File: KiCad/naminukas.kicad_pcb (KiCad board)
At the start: 2 copper layers, 10 parts, among them U1 TPSM63606RDLR

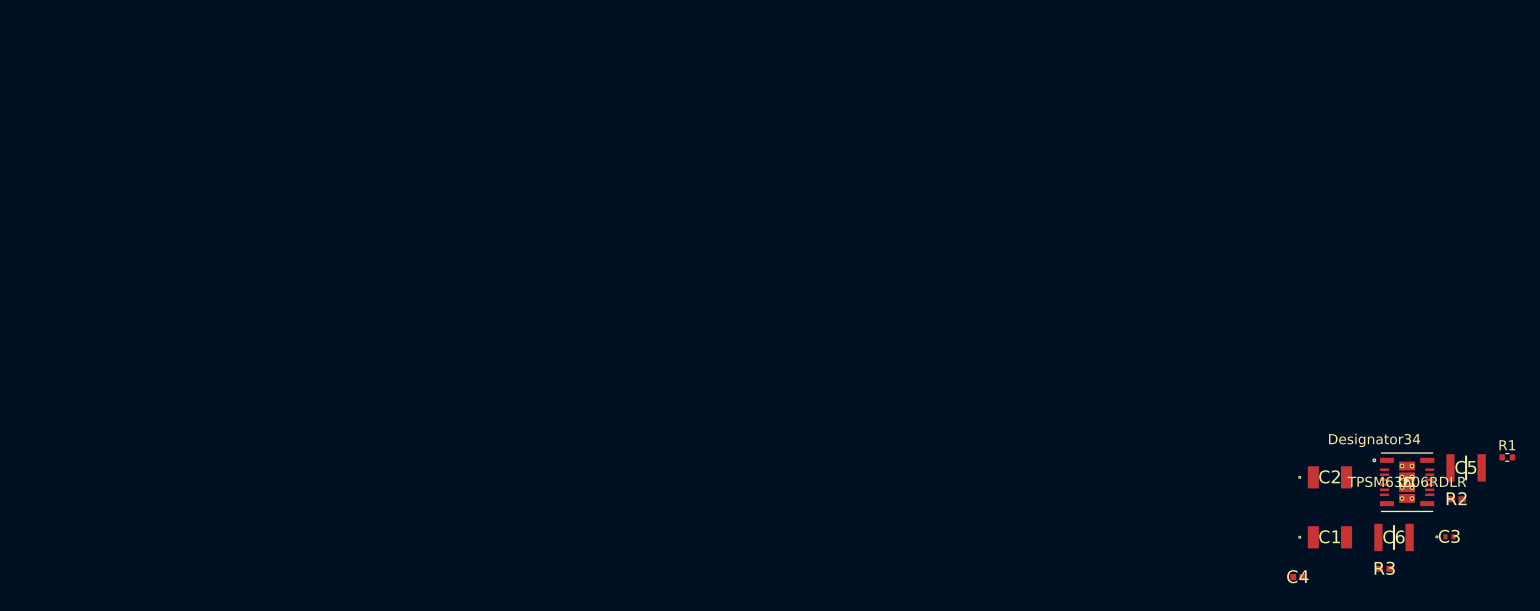
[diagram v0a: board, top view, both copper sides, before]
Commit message: feat(pcb): add mounting holes
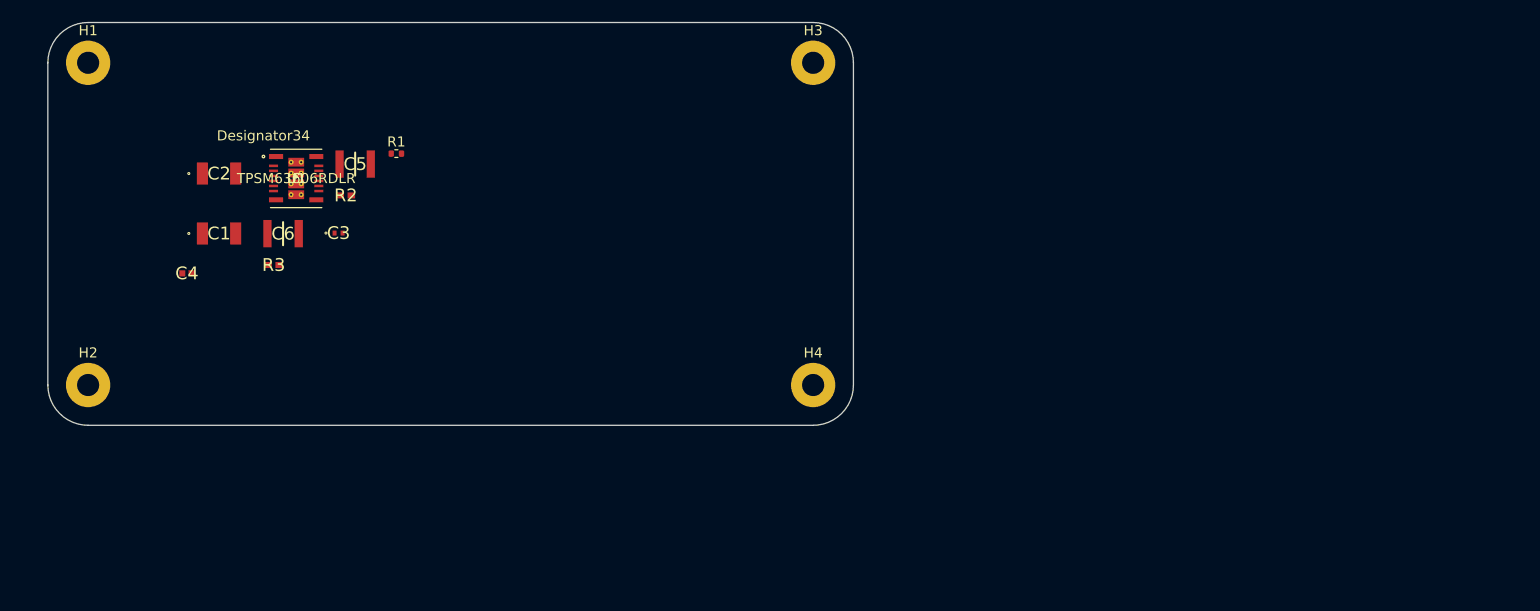
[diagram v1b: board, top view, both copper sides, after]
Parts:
- added H1: Mounting hole, MountingHole:MountingHole_2.2mm_M2_Pad, F.Cu at (24.0, 24.0)
- added H2: Mounting hole, MountingHole:MountingHole_2.2mm_M2_Pad, F.Cu at (24.0, 56.0)
- added H3: Mounting hole, MountingHole:MountingHole_2.2mm_M2_Pad, F.Cu at (96.0, 24.0)
- added H4: Mounting hole, MountingHole:MountingHole_2.2mm_M2_Pad, F.Cu at (96.0, 56.0)
- moved U1 114.4 mm to (44.7, 35.5)
- moved C6 114.4 mm to (43.4, 41.0)
- moved R1 114.4 mm to (54.6, 33.0)
- moved R3 114.4 mm to (42.4, 44.1)
- moved C1 114.4 mm to (37.0, 41.0)
- moved C2 114.4 mm to (37.0, 35.0)
- moved C3 114.4 mm to (48.9, 40.9)
- moved C4 114.4 mm to (33.8, 44.9)
- moved C5 114.4 mm to (50.5, 34.1)
- moved R2 114.4 mm to (49.6, 37.2)
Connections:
- C1 pad 1: GNDREF -> GND
- C2 pad 1: GNDREF -> GND
- C3 pad 1: GNDREF -> GND
- C5 pad 1: GNDREF -> GND
- C6 pad 1: GNDREF -> GND
- R1 pad 2: GNDREF -> GND
- R3 pad 1: GNDREF -> GND
- U1 pad 17: GNDREF -> GND
- U1 pad 18: GNDREF -> GND
- U1 pad 19: GNDREF -> GND
- U1 pad 20: GNDREF -> GND
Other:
- board outline added: 80 x 40 mm
- copper layers 2 -> 4

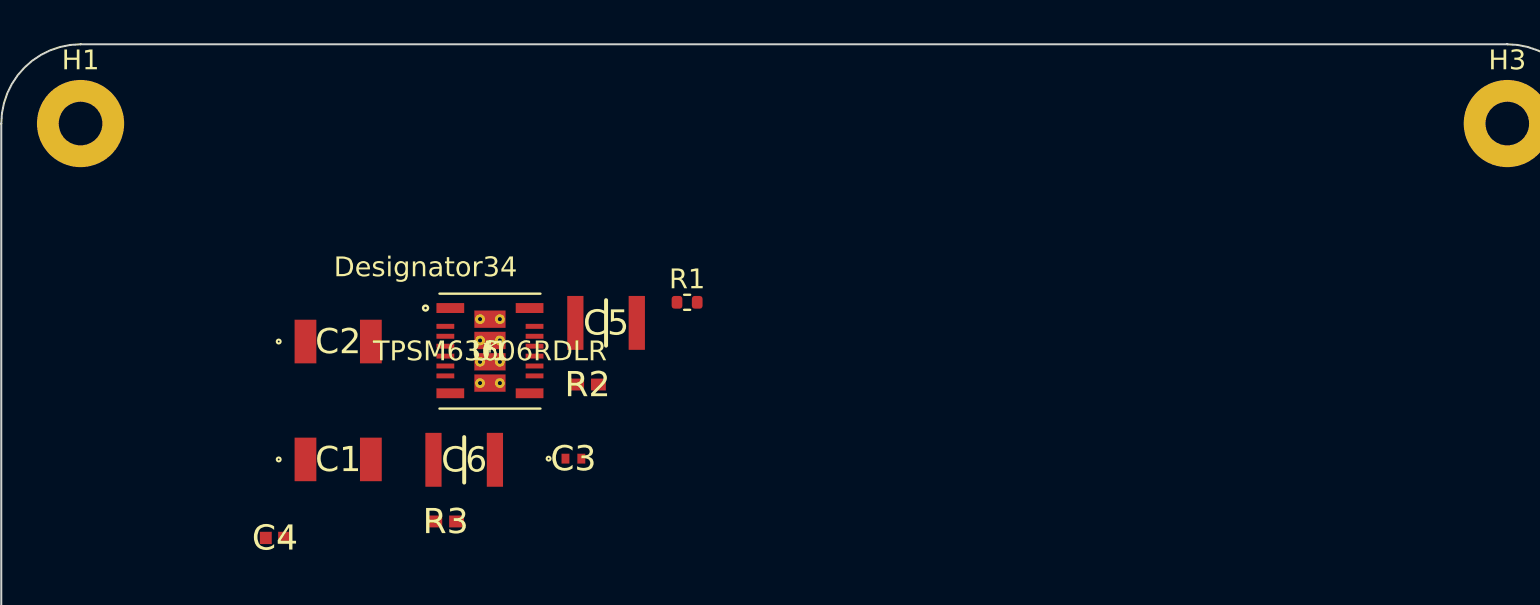
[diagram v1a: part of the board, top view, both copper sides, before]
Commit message: feat(pcb): add schematic for connectors
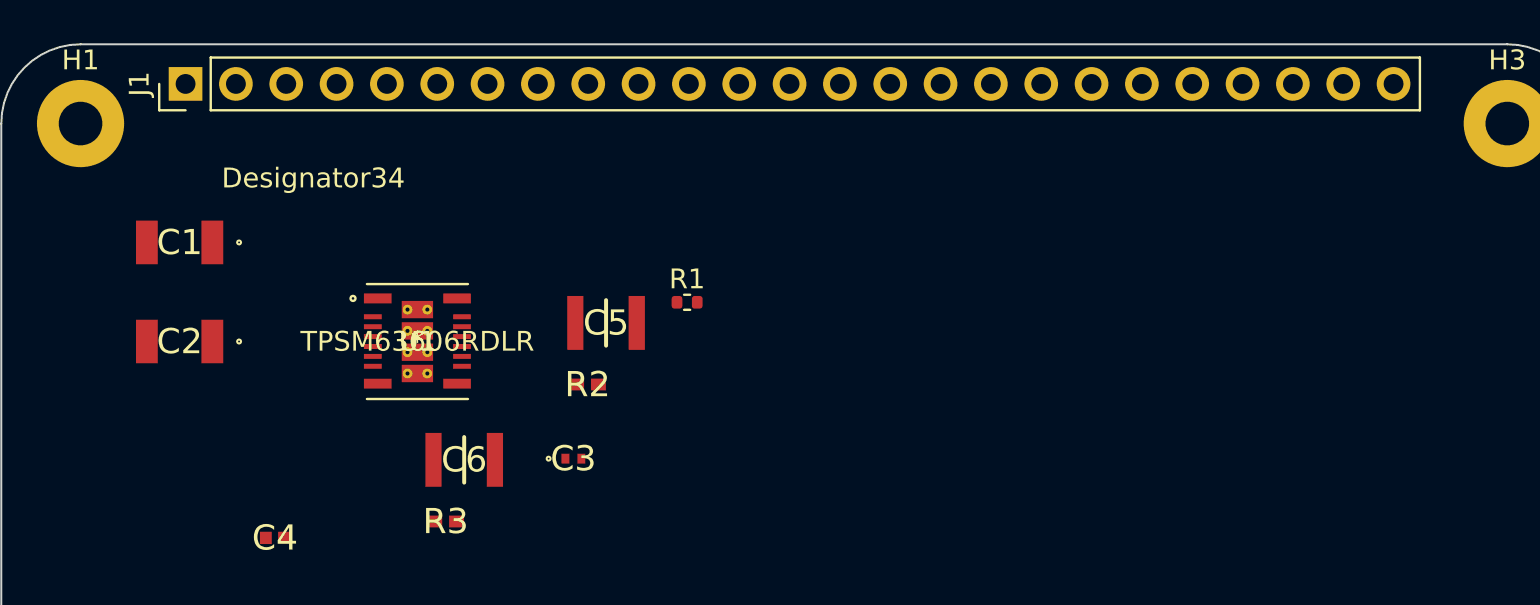
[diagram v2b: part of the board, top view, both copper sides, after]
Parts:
- added J1: Conn_01x25, Connector_PinHeader_2.54mm:PinHeader_1x25_P2.54mm_Vertical, F.Cu at (29.3, 22.0)
- moved C1 13.6 mm to (29.0, 30.0), turned to 180 degrees
- moved C2 8.00 mm to (29.0, 35.0), turned to 180 degrees
- moved U1 3.69 mm to (41.0, 35.0)

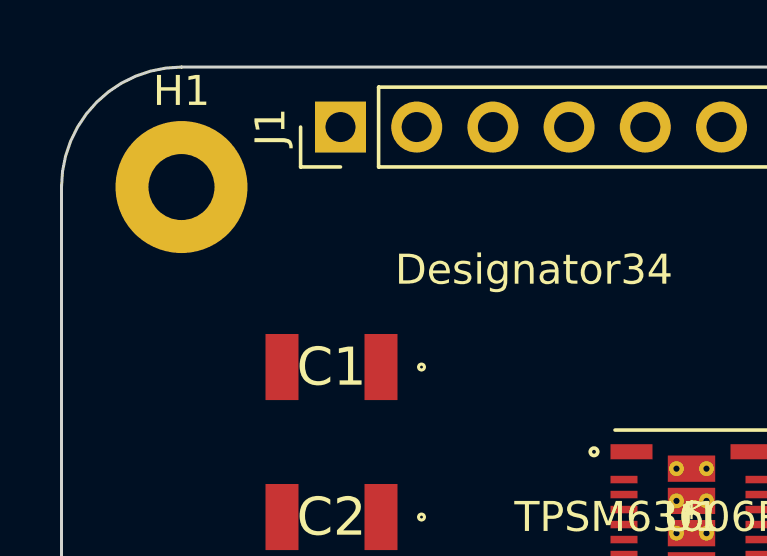
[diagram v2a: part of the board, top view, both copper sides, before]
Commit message: feat(pcb): make layer 2 copper ground plane
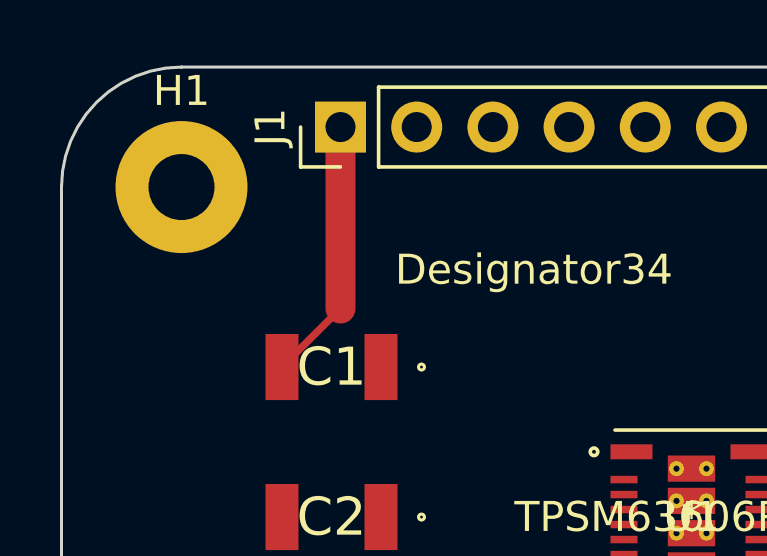
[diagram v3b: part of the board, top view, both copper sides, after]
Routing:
- net +BATT: track 0.00 -> 8.81 mm
- added copper zone on In1.Cu, net GND
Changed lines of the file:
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@@
   (gr_line (start 100 24) (end 100 56) (layer "Edge.Cuts") (width 0.1))
   (gr_arc (start 24 60) (mid 21.171573 58.828427) (end 20 56) (layer "Edge.Cuts") (width 0.1))
+  (segment (start 29.3 22) (end 29.3 28.05) (width 1) (layer "F.Cu") (net 1))
+  (segment (start 29.3 28.05) (end 27.35 30) (width 0.25) (layer "F.Cu") (net 1))
+  (zone (net 7) (net_name "GND") (layer "In1.Cu") (hatch edge 0.508)
+    (connect_pads (clearance 0.508))
+    (min_thickness 0.254) (filled_areas_thickness no)
+    (fill yes (thermal_gap 0.508) (thermal_bridge_width 0.508))
+    (polygon
+      (pts
+        (xy 100 60)
+        (xy 20 60)
+        (xy 20 20)
+        (xy 100 20)
+      )
+    )
+  )
 )

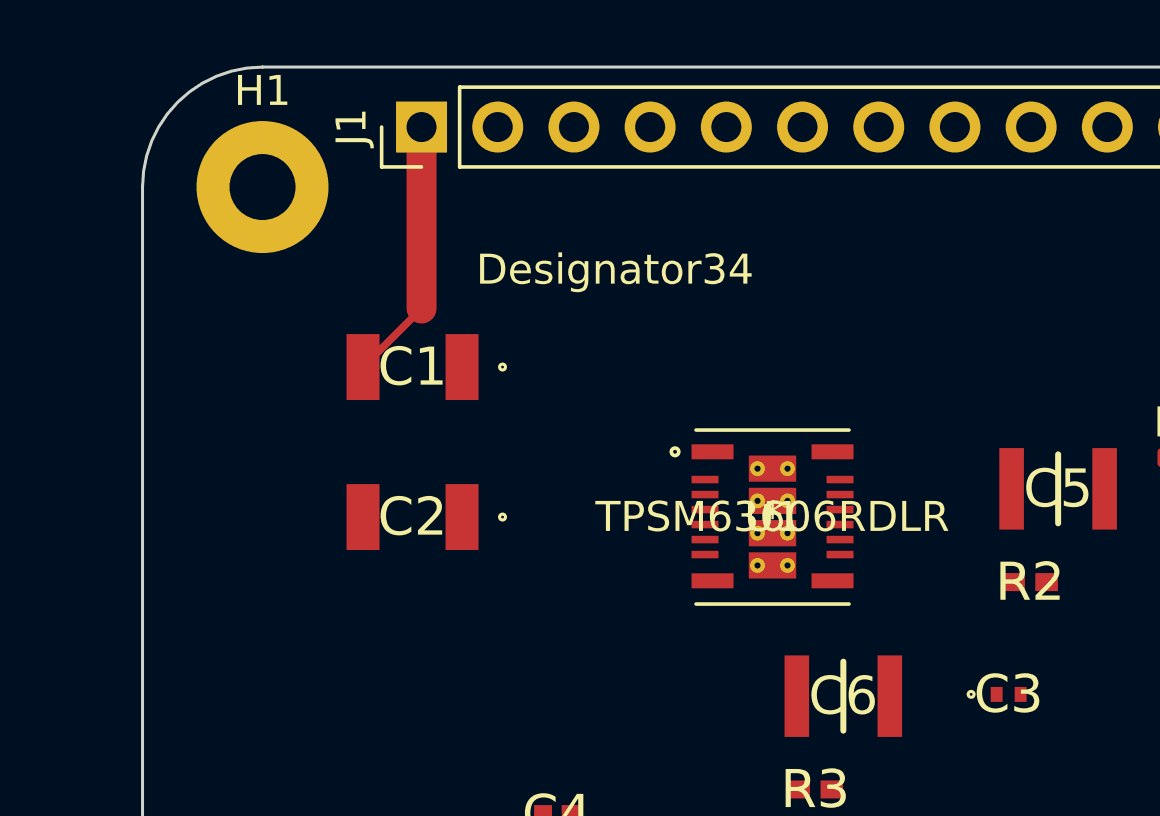
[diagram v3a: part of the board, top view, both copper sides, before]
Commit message: chore(pcb): start drawing tracks
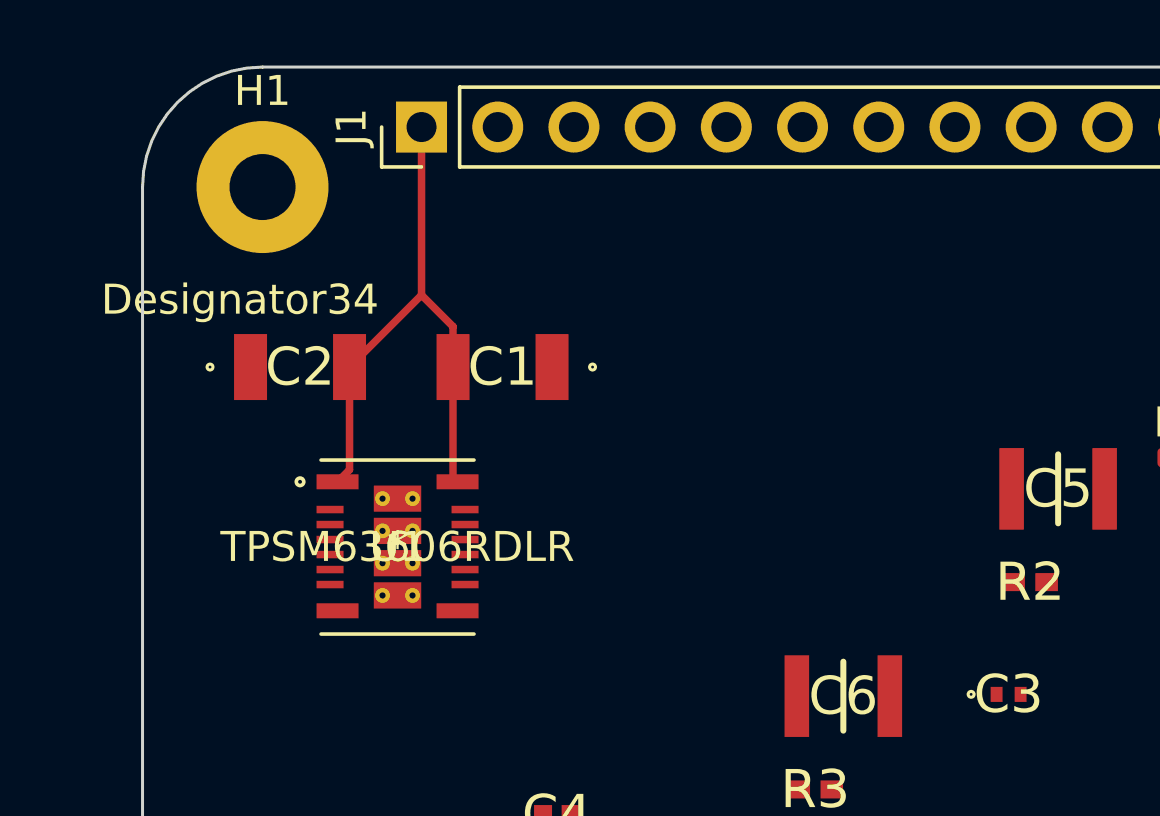
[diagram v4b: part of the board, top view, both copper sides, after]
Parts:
- moved U1 12.5 mm to (28.5, 36.0)
- moved C2 6.25 mm to (25.2, 30.0), turned to 0 degrees
- moved C1 3.00 mm to (32.0, 30.0)
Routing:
- net +BATT: track 8.81 -> 19.7 mm
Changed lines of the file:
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@@
   )
   (footprint "C3225X7R1H106M250AC:C3225_Commercial" (layer "F.Cu")
-    (at 29 35 180)
+    (at 25.25 30)
     (descr "C3225_Commercial")
     (tags "Capacitor")
@@
     (fp_line (start 1.6 -1.25) (end 1.6 1.25) (layer "F.Fab") (width 0.2))
     (fp_line (start 1.6 1.25) (end -1.6 1.25) (layer "F.Fab") (width 0.2))
-    (pad "1" smd rect locked (at -1.65 0 180) (size 1.1 2.2) (layers "F.Cu" "F.Paste" "F.Mask")
+    (pad "1" smd rect locked (at -1.65 0) (size 1.1 2.2) (layers "F.Cu" "F.Paste" "F.Mask")
       (net 7 "GND") (pintype "passive"))
-    (pad "2" smd rect locked (at 1.65 0 180) (size 1.1 2.2) (layers "F.Cu" "F.Paste" "F.Mask")
+    (pad "2" smd rect locked (at 1.65 0) (size 1.1 2.2) (layers "F.Cu" "F.Paste" "F.Mask")
       (net 1 "+BATT") (pintype "passive"))
     (model "C3225X7R1H106M250AC.stp"
@@
   )
   (footprint "C3225X7R1H106M250AC:C3225_Commercial" (layer "F.Cu")
-    (at 29 30 180)
+    (at 32 30 180)
     (descr "C3225_Commercial")
     (tags "Capacitor")
@@
   )
   (footprint "Power module:RDL0020A-MFG" (layer "F.Cu")
-    (at 41 35)
+    (at 28.5 36)
     (property "Sheetfile" "power-5V.kicad_sch")
     (property "Sheetname" "Power 5V")
@@
   (gr_line (start 100 24) (end 100 56) (layer "Edge.Cuts") (width 0.1))
   (gr_arc (start 24 60) (mid 21.171573 58.828427) (end 20 56) (layer "Edge.Cuts") (width 0.1))
-  (segment (start 29.3 22) (end 29.3 28.05) (width 1) (layer "F.Cu") (net 1))
-  (segment (start 29.3 28.05) (end 27.35 30) (width 0.25) (layer "F.Cu") (net 1))
+  (segment (start 30.35 30) (end 30.35 33.675) (width 0.25) (layer "F.Cu") (net 1))
+  (segment (start 26.9 30) (end 26.9 33.425) (width 0.25) (layer "F.Cu") (net 1))
+  (segment (start 29.3 27.6) (end 26.9 30) (width 0.25) (layer "F.Cu") (net 1))
+  (segment (start 29.3 27.6) (end 30.35 28.65) (width 0.25) (layer "F.Cu") (net 1))
+  (segment (start 30.35 28.65) (end 30.35 30) (width 0.25) (layer "F.Cu") (net 1))
+  (segment (start 29.3 22) (end 29.3 27.6) (width 0.25) (layer "F.Cu") (net 1))
+  (segment (start 30.35 33.675) (end 30.500001 33.825001) (width 0.25) (layer "F.Cu") (net 1))
+  (segment (start 26.9 33.425) (end 26.499999 33.825001) (width 0.25) (layer "F.Cu") (net 1))
   (zone (net 7) (net_name "GND") (layer "In1.Cu") (hatch edge 0.508)
     (connect_pads (clearance 0.508))
